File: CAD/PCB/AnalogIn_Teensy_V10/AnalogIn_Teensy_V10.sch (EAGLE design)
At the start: 93 parts, among them IC1 AD8599R, IC2 AD8599R, IC3 AD8599R, IC4 AD8599R, U1 AD7327BRUZ, U2 SN65HVD31DR, U3 SN65HVD31DR

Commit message: Update TeensyV10 board
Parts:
- removed C1, C2, C3: 4.7uf, SparkFun-Capacitors:CAP1206
- removed R4: 22, SparkFun-Resistors:RESISTOR1206
- added C41, C42, C43, C44, C45, C46, C47, C48: (no value), SparkFun-Capacitors:CAP0603-CAP
- added C49: 10uf, SparkFun-Capacitors:CAP0603-CAP
- added C50, C51: 0.1uf, SparkFun-Capacitors:CAP0603-CAP
- added R29, R31, R32, R33, R34, R35, R36: (no value), SparkFun-Resistors:RESISTOR0603
- added R30: 50, SparkFun-Resistors:RESISTOR0603
- added R37: 22, SparkFun-Resistors:RESISTOR0603
- C13, C14: value 0.1uf -> 4.7uf; device SparkFun-Capacitors:CAP1206 -> SparkFun-Capacitors:CAP0603-CAP
- C4, C5, C6: device SparkFun-Capacitors:CAP1206 -> SparkFun-Capacitors:CAP0603-CAP
- C7: value 10uf -> 4.7uf; device SparkFun-Capacitors:CAP1206 -> SparkFun-Capacitors:CAP0603-CAP
- C8: value 680nf -> 680nF; device SparkFun-Capacitors:CAP1206 -> SparkFun-Capacitors:CAP0603-CAP
- R1, R11, R12, R14, R16, R17, R18, R2, R20, R21, R23, R24, R26, R27, R3, R6, R8, R9: device SparkFun-Resistors:RESISTOR1206 -> SparkFun-Resistors:RESISTOR0603
- R10, R13, R15, R19, R22, R25, R28, R7: value 50 -> 180; device SparkFun-Resistors:RESISTOR1206 -> SparkFun-Resistors:RESISTOR0603
- R5: value 50 -> (none); device SparkFun-Resistors:RESISTOR1206 -> SparkFun-Resistors:RESISTOR0603
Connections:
- net +V12 renamed +VOUT
- net -V12 renamed -VOUT
- removed net N$18: C12.1, C19.1, IC1P.V+
- removed net N$19: C20.1, C21.1, IC1P.V-
- removed net N$26: C24.1, C25.1, IC2P.V+
- removed net N$27: C26.1, C27.1, IC2P.V-
- removed net N$34: C30.1, C31.1, IC3P.V+
- removed net N$35: C32.1, C33.1, IC3P.V-
- removed net N$42: C36.1, C37.1, IC4P.V+
- removed net N$43: C38.1, C39.1, IC4P.V-
- net ADC_CS: now also R3.1; no longer R4.1
- net AGND: now also C41.2, C42.2, C43.2, C44.2, C45.2, C46.2, C47.2, C48.2, C49.2, C50.2, C51.2, C8.1, C9.2, R29.1, R31.1, R32.1, R33.1, R34.1, R35.1, R36.1, R5.1; no longer C13.2, C14.2, C7.2, C8.2
- net AIN0: now also R30.1; no longer R5.1
- net AIN7: now also R24.1; no longer R26.1
- net DGND: now also C13.1, C14.2, C7.2; no longer C1.2, C2.1, C3.2
- net MISO: now also R1.1; no longer R2.1
- net MOSI: now also R37.1; no longer R1.1
- net N$10: now also R37.2; no longer R1.2
- net N$11: now also R1.2; no longer R2.2
- net N$12: now also C14.1; no longer C1.1
- net N$13: now also R3.2; no longer R4.2
- net N$14: now also C41.1, R30.2; no longer R5.2
- net N$15: now also R2.2; no longer R3.2
- net N$16: now also R5.2
- net N$20: now also C42.1
- net N$21: now also R29.2
- net N$23: now also C43.1
- net N$24: now also R31.2
- net N$28: now also C44.1
- net N$29: now also R16.1, R32.2; no longer R15.1
- net N$30: now also R15.1, R16.2; no longer R15.2, R16.1
- net N$31: now also C45.1
- net N$32: now also R33.2
- net N$36: now also C46.1
- net N$37: now also R34.2
- net N$39: now also C47.1
- net N$40: now also R26.1, R35.2; no longer R24.1
- net N$41: now also R26.2; no longer R24.2
- net N$44: now also C48.1, R24.2; no longer R26.2
- net N$45: now also R36.2
- net REF: now also C8.2; no longer C8.1
- net SCLK: now also R2.1; no longer R3.1
- net V+12: now also C12.1, C19.1, C24.1, C25.1, C30.1, C31.1, C36.1, C37.1, C7.1, IC1P.V+, IC2P.V+, IC3P.V+, IC4P.V+; no longer C3.1
- net V-12: now also C13.2, C20.1, C21.1, C26.1, C27.1, C32.1, C33.1, C38.1, C39.1, C49.1, C50.1, IC1P.V-, IC2P.V-, IC3P.V-, IC4P.V-; no longer C2.2, C6.1, C7.1
- net V3IN: now also R15.2; no longer R16.2
- net VDD: now also C6.1; no longer C13.1
- net VSS: now also C51.1; no longer C14.1
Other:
- moved on the sheet: C10, C11, C12, C13, C14, C15, C16, C17, C18, C19, C20, C21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

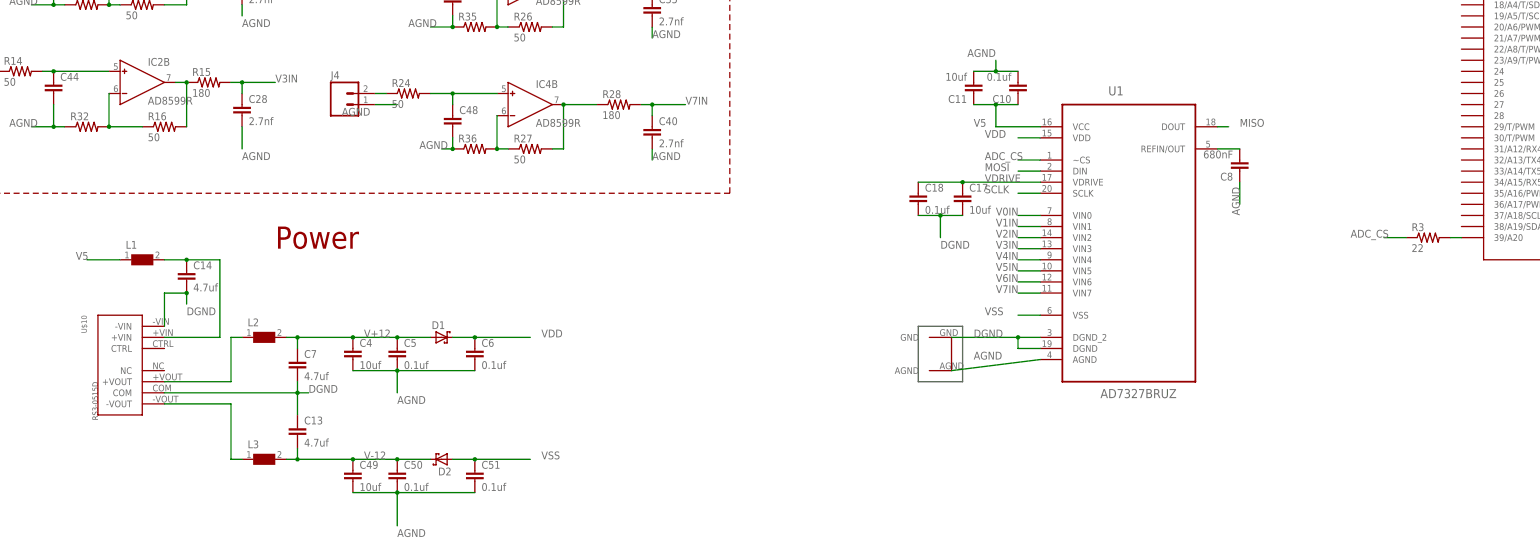
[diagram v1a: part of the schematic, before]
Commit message: Update Teensy verion
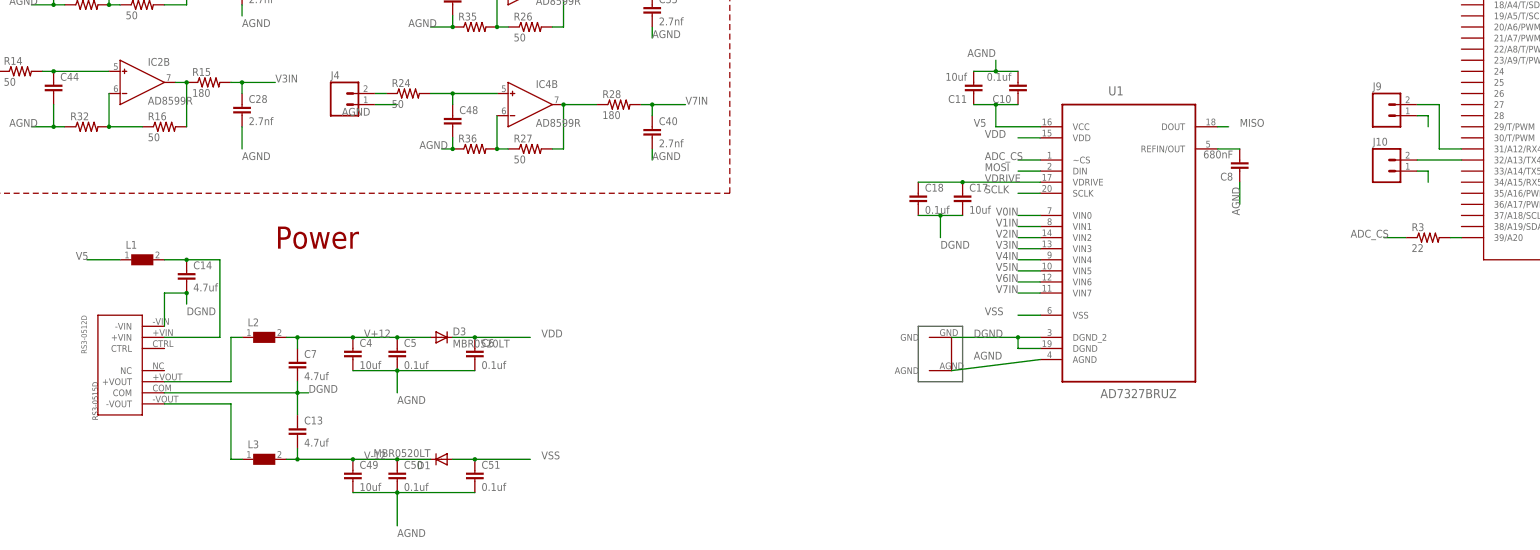
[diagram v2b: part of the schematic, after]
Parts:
- removed D2: (no value), diode:SCHOTTKY-DIODESMD
- added D3: MBR0520LT, diode:MBR0520LT
- added J10, J9: (no value), SparkFun-Connectors:M023.5MM
- D1: value (none) -> MBR0520LT; device diode:SCHOTTKY-DIODESMD -> diode:MBR0520LT
- renumbered U$10 to RS3-0512D
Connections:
- new net N$18: J9.2, U$9.31/A12/RX4
- new net N$19: J10.2, U$9.32/A13/TX4
- net DGND: now also J10.1, J9.1
- net V+12: now also D3.A; no longer D1.A
- net V-12: now also D1.C; no longer D2.C
- net VDD: now also D3.C; no longer D1.C
- net VSS: now also D1.A; no longer D2.A
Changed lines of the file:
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@@
 <part name="C10" library="SparkFun-Capacitors" deviceset="CAP" device="0603-CAP" value="0.1uf"/>
 <part name="C11" library="SparkFun-Capacitors" deviceset="CAP" device="0603-CAP" value="10uf"/>
-<part name="D1" library="diode" deviceset="SCHOTTKY-DIODE" device="SMD"/>
 <part name="U2" library="Joshparts4" deviceset="SN65HVD31DR" device=""/>
 <part name="U3" library="Joshparts4" deviceset="SN65HVD31DR" device=""/>
@@
 <part name="C17" library="SparkFun-Capacitors" deviceset="CAP" device="0603-CAP" value="10uf"/>
 <part name="C18" library="SparkFun-Capacitors" deviceset="CAP" device="0603-CAP" value="0.1uf"/>
-<part name="D2" library="diode" deviceset="SCHOTTKY-DIODE" device="SMD"/>
 <part name="U$4" library="Joshparts2" deviceset="GNDPLANESHRT" device=""/>
 <part name="J5" library="SparkFun-Connectors" deviceset="M02" device="3.5MM"/>
@@
 <part name="U$9" library="Teensy_3_and_LC_Series_Boards_v1.4" deviceset="TEENSY_3.6_DIL" device=""/>
 <part name="FRAME1" library="frames" deviceset="A3L-LOC" device=""/>
-<part name="U$10" library="JoshParts10" deviceset="RS3-0515D" device=""/>
+<part name="RS3-0512D" library="JoshParts10" deviceset="RS3-0515D" device=""/>
 <part name="IC1" library="analog-devices" deviceset="AD8599" device="R"/>
 <part name="C9" library="SparkFun-Capacitors" deviceset="CAP" device="0603-CAP" value="2.7nf"/>
@@
 <part name="R2" library="SparkFun-Resistors" deviceset="RESISTOR" device="0603" value="22"/>
 <part name="R3" library="SparkFun-Resistors" deviceset="RESISTOR" device="0603" value="22"/>
+<part name="D3" library="diode" deviceset="MBR0520LT" device=""/>
+<part name="D1" library="diode" deviceset="MBR0520LT" device=""/>
+<part name="J9" library="SparkFun-Connectors" deviceset="M02" device="3.5MM"/>
+<part name="J10" library="SparkFun-Connectors" deviceset="M02" device="3.5MM"/>
 </parts>
 <sheets>
@@
 <instance part="C10" gate="G$1" x="259.08" y="111.76" rot="R180"/>
 <instance part="C11" gate="G$1" x="248.92" y="111.76" rot="R180"/>
-<instance part="D1" gate="G$1" x="127" y="53.34"/>
 <instance part="U2" gate="G$1" x="254" y="226.06"/>
 <instance part="U3" gate="G$1" x="254" y="190.5"/>
@@
 <instance part="C17" gate="G$1" x="246.38" y="83.82"/>
 <instance part="C18" gate="G$1" x="236.22" y="83.82"/>
-<instance part="D2" gate="G$1" x="127" y="25.4" rot="R180"/>
 <instance part="U$4" gate="G$1" x="243.84" y="53.34" rot="R180"/>
 <instance part="J5" gate="G$1" x="12.7" y="208.28"/>
@@
 <instance part="U$9" gate="G$1" x="388.62" y="124.46"/>
 <instance part="FRAME1" gate="G$1" x="0" y="0"/>
-<instance part="U$10" gate="G$1" x="58.42" y="35.56" rot="MR270"/>
+<instance part="RS3-0512D" gate="G$1" x="58.42" y="35.56" rot="MR270"/>
 <instance part="IC1" gate="A" x="55.88" y="208.28"/>
 <instance part="IC1" gate="B" x="55.88" y="185.42"/>
@@
 <instance part="R2" gate="G$1" x="347.98" y="137.16"/>
 <instance part="R3" gate="G$1" x="353.06" y="76.2"/>
+<instance part="D3" gate="G$1" x="127" y="53.34"/>
+<instance part="D1" gate="G$1" x="127" y="25.4" rot="R180"/>
+<instance part="J9" gate="G$1" x="342.9" y="104.14"/>
+<instance part="J10" gate="G$1" x="342.9" y="91.44"/>
 </instances>
 <busses>
@@
 <net name="VDD" class="0">
 <segment>
-<pinref part="D1" gate="G$1" pin="C"/>
 <wire x1="129.54" y1="53.34" x2="134.62" y2="53.34" width="0.1524" layer="91"/>
 <label x="149.86" y="53.34" size="1.778" layer="95"/>
@@
 <wire x1="134.62" y1="53.34" x2="147.32" y2="53.34" width="0.1524" layer="91"/>
 <junction x="134.62" y="53.34"/>
+<pinref part="D3" gate="G$1" pin="C"/>
 </segment>
 <segment>
@@
 <wire x1="129.54" y1="25.4" x2="134.62" y2="25.4" width="0.1524" layer="91"/>
 <label x="149.86" y="25.4" size="1.778" layer="95"/>
-<pinref part="D2" gate="G$1" pin="A"/>
 <pinref part="C51" gate="G$1" pin="1"/>
 <wire x1="134.62" y1="25.4" x2="147.32" y2="25.4" width="0.1524" layer="91"/>
 <junction x="134.62" y="25.4"/>
+<pinref part="D1" gate="G$1" pin="A"/>
 </segment>
 <segment>
@@
 <wire x1="76.2" y1="71.12" x2="76.2" y2="53.34" width="0.1524" layer="91"/>
 <wire x1="76.2" y1="53.34" x2="63.5" y2="53.34" width="0.1524" layer="91"/>
-<pinref part="U$10" gate="G$1" pin="+VIN"/>
+<pinref part="RS3-0512D" gate="G$1" pin="+VIN"/>
 <pinref part="C14" gate="G$1" pin="1"/>
 <junction x="68.58" y="71.12"/>
@@
 <wire x1="78.74" y1="43.18" x2="78.74" y2="53.34" width="0.1524" layer="91"/>
 <pinref part="L2" gate="G$1" pin="1"/>
-<pinref part="U$10" gate="G$1" pin="+VOUT"/>
+<pinref part="RS3-0512D" gate="G$1" pin="+VOUT"/>
 <wire x1="63.5" y1="43.18" x2="78.74" y2="43.18" width="0.1524" layer="91"/>
 </segment>
@@
 <pinref part="L3" gate="G$1" pin="1"/>
 <wire x1="78.74" y1="25.4" x2="81.28" y2="25.4" width="0.1524" layer="91"/>
-<pinref part="U$10" gate="G$1" pin="-VOUT"/>
+<pinref part="RS3-0512D" gate="G$1" pin="-VOUT"/>
 <wire x1="63.5" y1="38.1" x2="78.74" y2="38.1" width="0.1524" layer="91"/>
 <wire x1="78.74" y1="38.1" x2="78.74" y2="25.4" width="0.1524" layer="91"/>
@@
 <wire x1="93.98" y1="40.64" x2="96.52" y2="40.64" width="0.1524" layer="91"/>
 <label x="96.52" y="40.64" size="1.778" layer="95"/>
-<pinref part="U$10" gate="G$1" pin="COM"/>
+<pinref part="RS3-0512D" gate="G$1" pin="COM"/>
 <pinref part="C7" gate="G$1" pin="2"/>
 <pinref part="C13" gate="G$1" pin="1"/>
@@
 <segment>
 <wire x1="68.58" y1="63.5" x2="63.5" y2="63.5" width="0.1524" layer="91"/>
-<pinref part="U$10" gate="G$1" pin="-VIN"/>
+<pinref part="RS3-0512D" gate="G$1" pin="-VIN"/>
 <wire x1="63.5" y1="63.5" x2="63.5" y2="55.88" width="0.1524" layer="91"/>
 <wire x1="68.58" y1="63.5" x2="68.58" y2="60.96" width="0.1524" layer="91"/>
@@
 <pinref part="C14" gate="G$1" pin="2"/>
 <junction x="68.58" y="63.5"/>
+</segment>
+<segment>
+<pinref part="J9" gate="G$1" pin="1"/>
+<wire x1="350.52" y1="104.14" x2="353.06" y2="104.14" width="0.1524" layer="91"/>
+<wire x1="353.06" y1="104.14" x2="353.06" y2="101.6" width="0.1524" layer="91"/>
+</segment>
+<segment>
+<pinref part="J10" gate="G$1" pin="1"/>
+<wire x1="350.52" y1="91.44" x2="353.06" y2="91.44" width="0.1524" layer="91"/>
+<wire x1="353.06" y1="91.44" x2="353.06" y2="88.9" width="0.1524" layer="91"/>
 </segment>
 </net>
@@
 <net name="V+12" class="0">
 <segment>
-<pinref part="D1" gate="G$1" pin="A"/>
 <label x="109.22" y="53.34" size="1.778" layer="95"/>
 <pinref part="C4" gate="G$1" pin="1"/>
@@
 <wire x1="93.98" y1="53.34" x2="93.98" y2="50.8" width="0.1524" layer="91"/>
 <junction x="93.98" y="53.34"/>
+<pinref part="D3" gate="G$1" pin="A"/>
 </segment>
 <segment>
@@
 <net name="V-12" class="0">
 <segment>
-<pinref part="D2" gate="G$1" pin="C"/>
 <label x="109.22" y="25.4" size="1.778" layer="95"/>
 <pinref part="C49" gate="G$1" pin="1"/>
@@
 <wire x1="93.98" y1="27.94" x2="93.98" y2="25.4" width="0.1524" layer="91"/>
 <junction x="93.98" y="25.4"/>
+<pinref part="D1" gate="G$1" pin="C"/>
 </segment>
 <segment>
@@
 </segment>
 </net>
+<net name="N$18" class="0">
+<segment>
+<pinref part="U$9" gate="G$1" pin="31/A12/RX4"/>
+<wire x1="360.68" y1="96.52" x2="355.6" y2="96.52" width="0.1524" layer="91"/>
+<wire x1="355.6" y1="96.52" x2="355.6" y2="106.68" width="0.1524" layer="91"/>
+<pinref part="J9" gate="G$1" pin="2"/>
+<wire x1="355.6" y1="106.68" x2="350.52" y2="106.68" width="0.1524" layer="91"/>
+</segment>
+</net>
+<net name="N$19" class="0">
+<segment>
+<pinref part="U$9" gate="G$1" pin="32/A13/TX4"/>
+<pinref part="J10" gate="G$1" pin="2"/>
+<wire x1="360.68" y1="93.98" x2="350.52" y2="93.98" width="0.1524" layer="91"/>
+</segment>
+</net>

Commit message: Teensy board
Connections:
- net N$18: now also J10.2, U$9.23/A9/T/PWM; no longer J9.2, U$9.31/A12/RX4
- net N$19: now also J9.2, U$9.22/A8/T/PWM; no longer J10.2, U$9.32/A13/TX4
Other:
- moved on the sheet: C10, C11, C13, C14, C15, C16, C17, C18, C4, C49, C5, C50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
